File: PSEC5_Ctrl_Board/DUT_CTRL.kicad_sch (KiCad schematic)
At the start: 2 parts, among them J2 QSH-040-01-X-D-DP-A, J4 QSH-040-01-X-D-DP-A

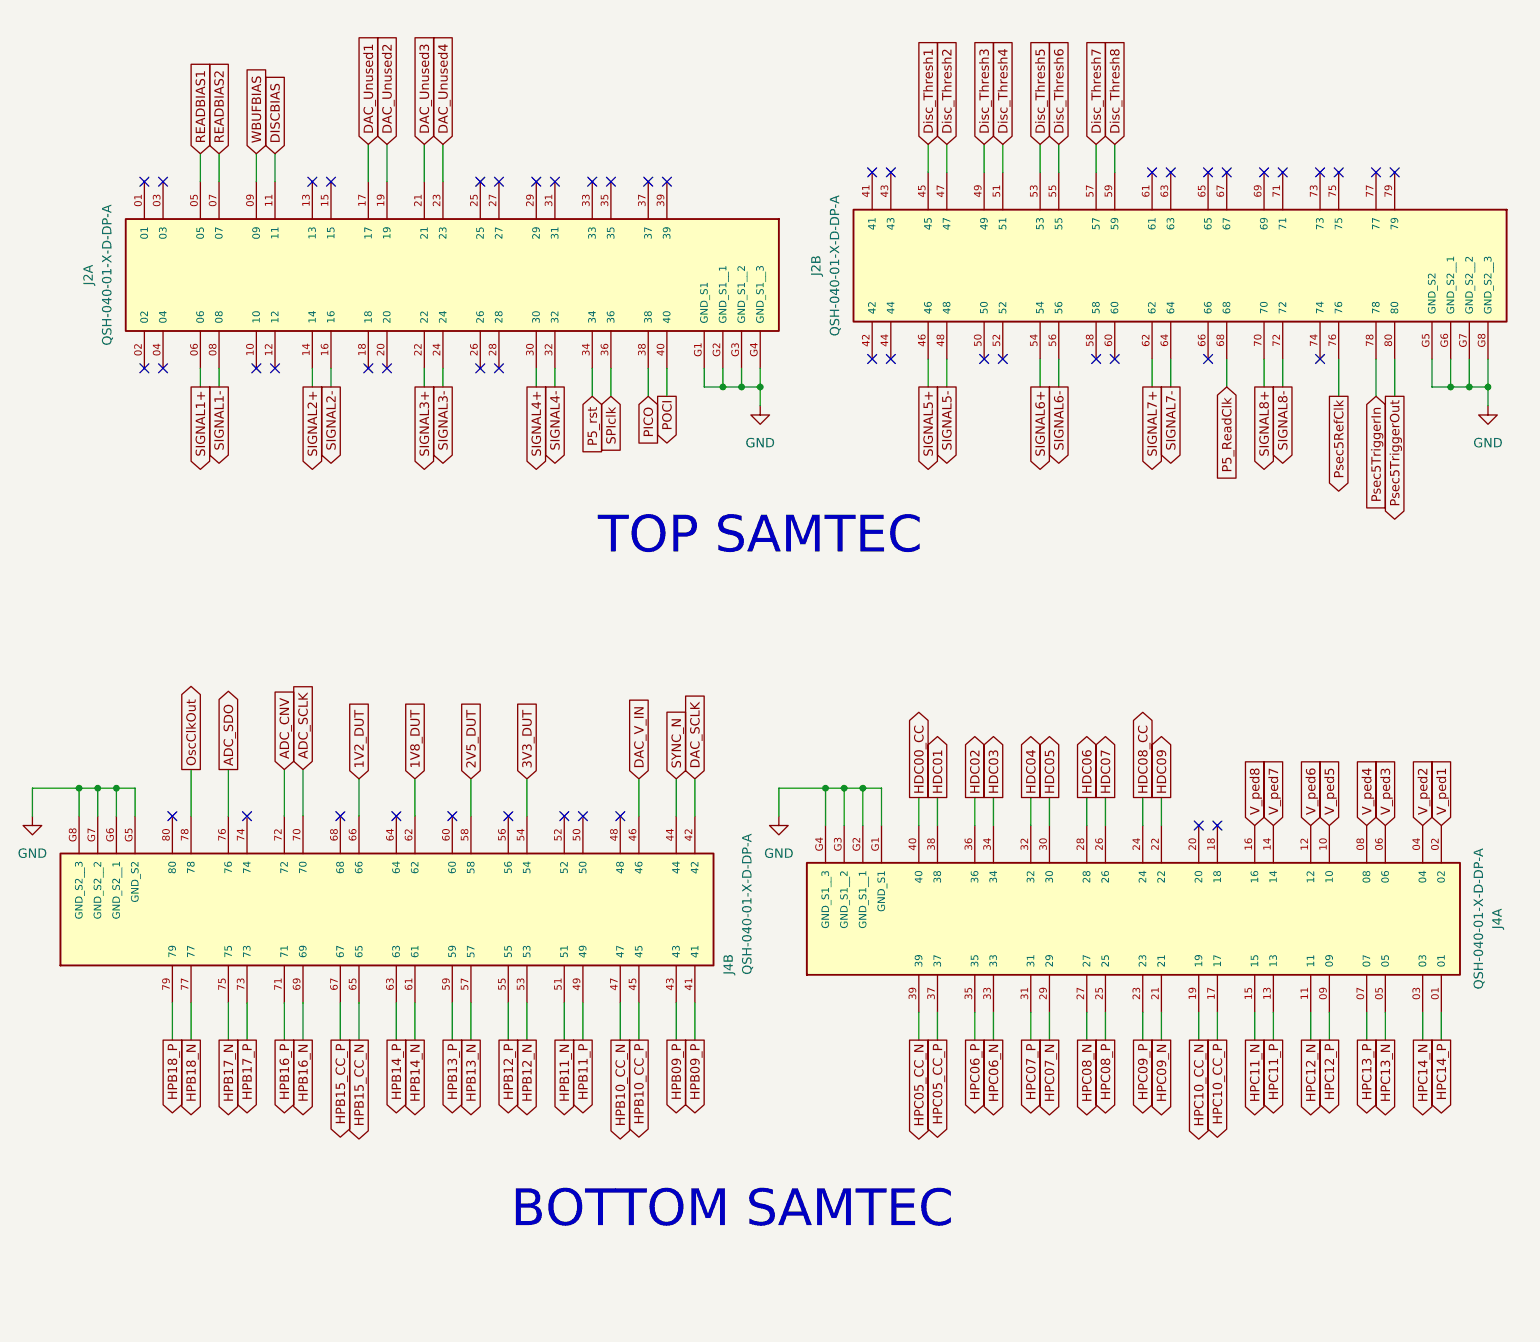
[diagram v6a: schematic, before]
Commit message: Changed Buck Regulators to external
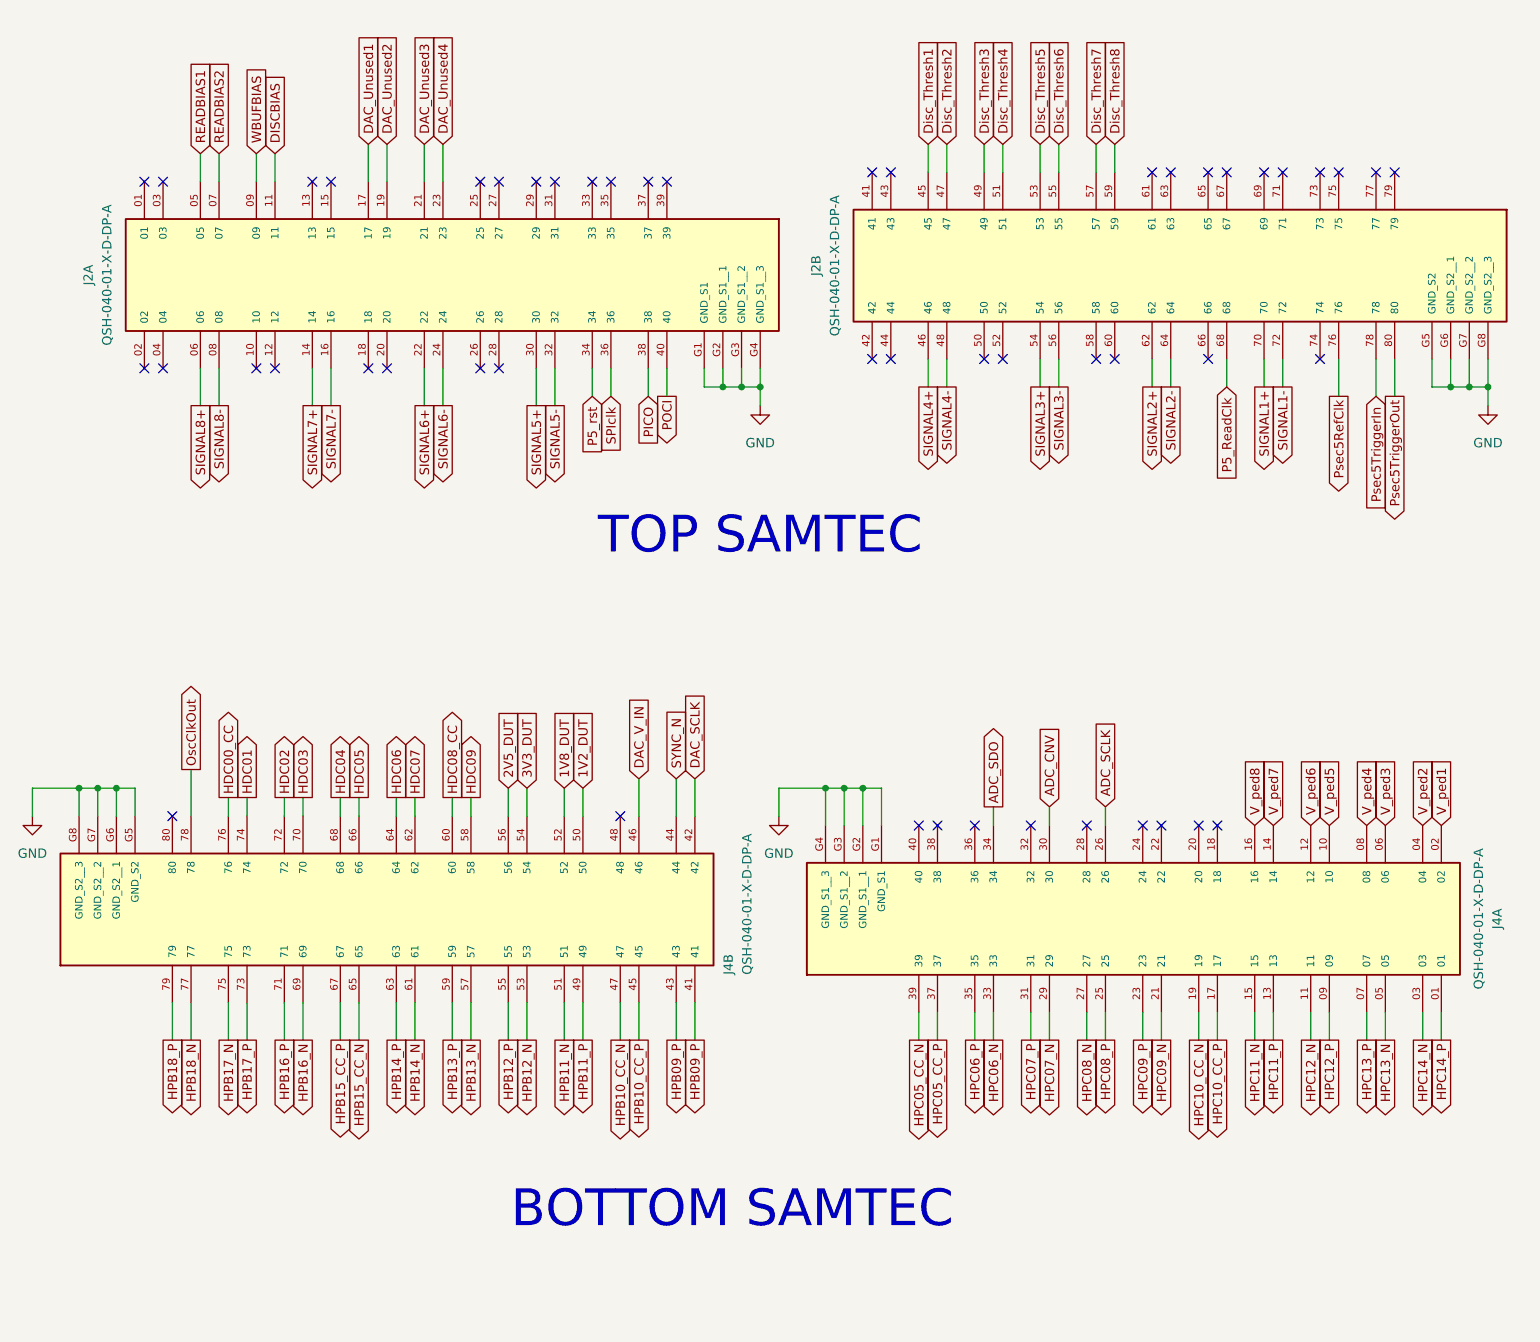
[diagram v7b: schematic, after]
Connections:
- net 1V2_DUT: now also J4.50; no longer J4.66
- net 1V8_DUT: now also J4.52; no longer J4.62
- net 2V5_DUT: now also J4.56; no longer J4.58
- net ADC_CNV: now also J4.30; no longer J4.72
- net ADC_SCLK: now also J4.26; no longer J4.70
- net ADC_SDO: now also J4.34; no longer J4.76
- net HDC00_CC: now also J4.76; no longer J4.40
- net HDC01: now also J4.74; no longer J4.38
- net HDC02: now also J4.72; no longer J4.36
- net HDC03: now also J4.70; no longer J4.34
- net HDC04: now also J4.68; no longer J4.32
- net HDC05: now also J4.66; no longer J4.30
- net HDC06: now also J4.64; no longer J4.28
- net HDC07: now also J4.62; no longer J4.26
- net HDC08_CC: now also J4.60; no longer J4.24
- net HDC09: now also J4.58; no longer J4.22
- net SIGNAL1+: now also J2.70; no longer J2.06
- net SIGNAL1-: now also J2.72; no longer J2.08
- net SIGNAL2+: now also J2.62; no longer J2.14
- net SIGNAL2-: now also J2.64; no longer J2.16
- net SIGNAL3+: now also J2.54; no longer J2.22
- net SIGNAL3-: now also J2.56; no longer J2.24
- net SIGNAL4+: now also J2.46; no longer J2.30
- net SIGNAL4-: now also J2.48; no longer J2.32
- net SIGNAL5+: now also J2.30; no longer J2.46
- net SIGNAL5-: now also J2.32; no longer J2.48
- net SIGNAL6+: now also J2.22; no longer J2.54
- net SIGNAL6-: now also J2.24; no longer J2.56
- net SIGNAL7+: now also J2.14; no longer J2.62
- net SIGNAL7-: now also J2.16; no longer J2.64
- net SIGNAL8+: now also J2.06; no longer J2.70
- net SIGNAL8-: now also J2.08; no longer J2.72

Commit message: rearranged samtec
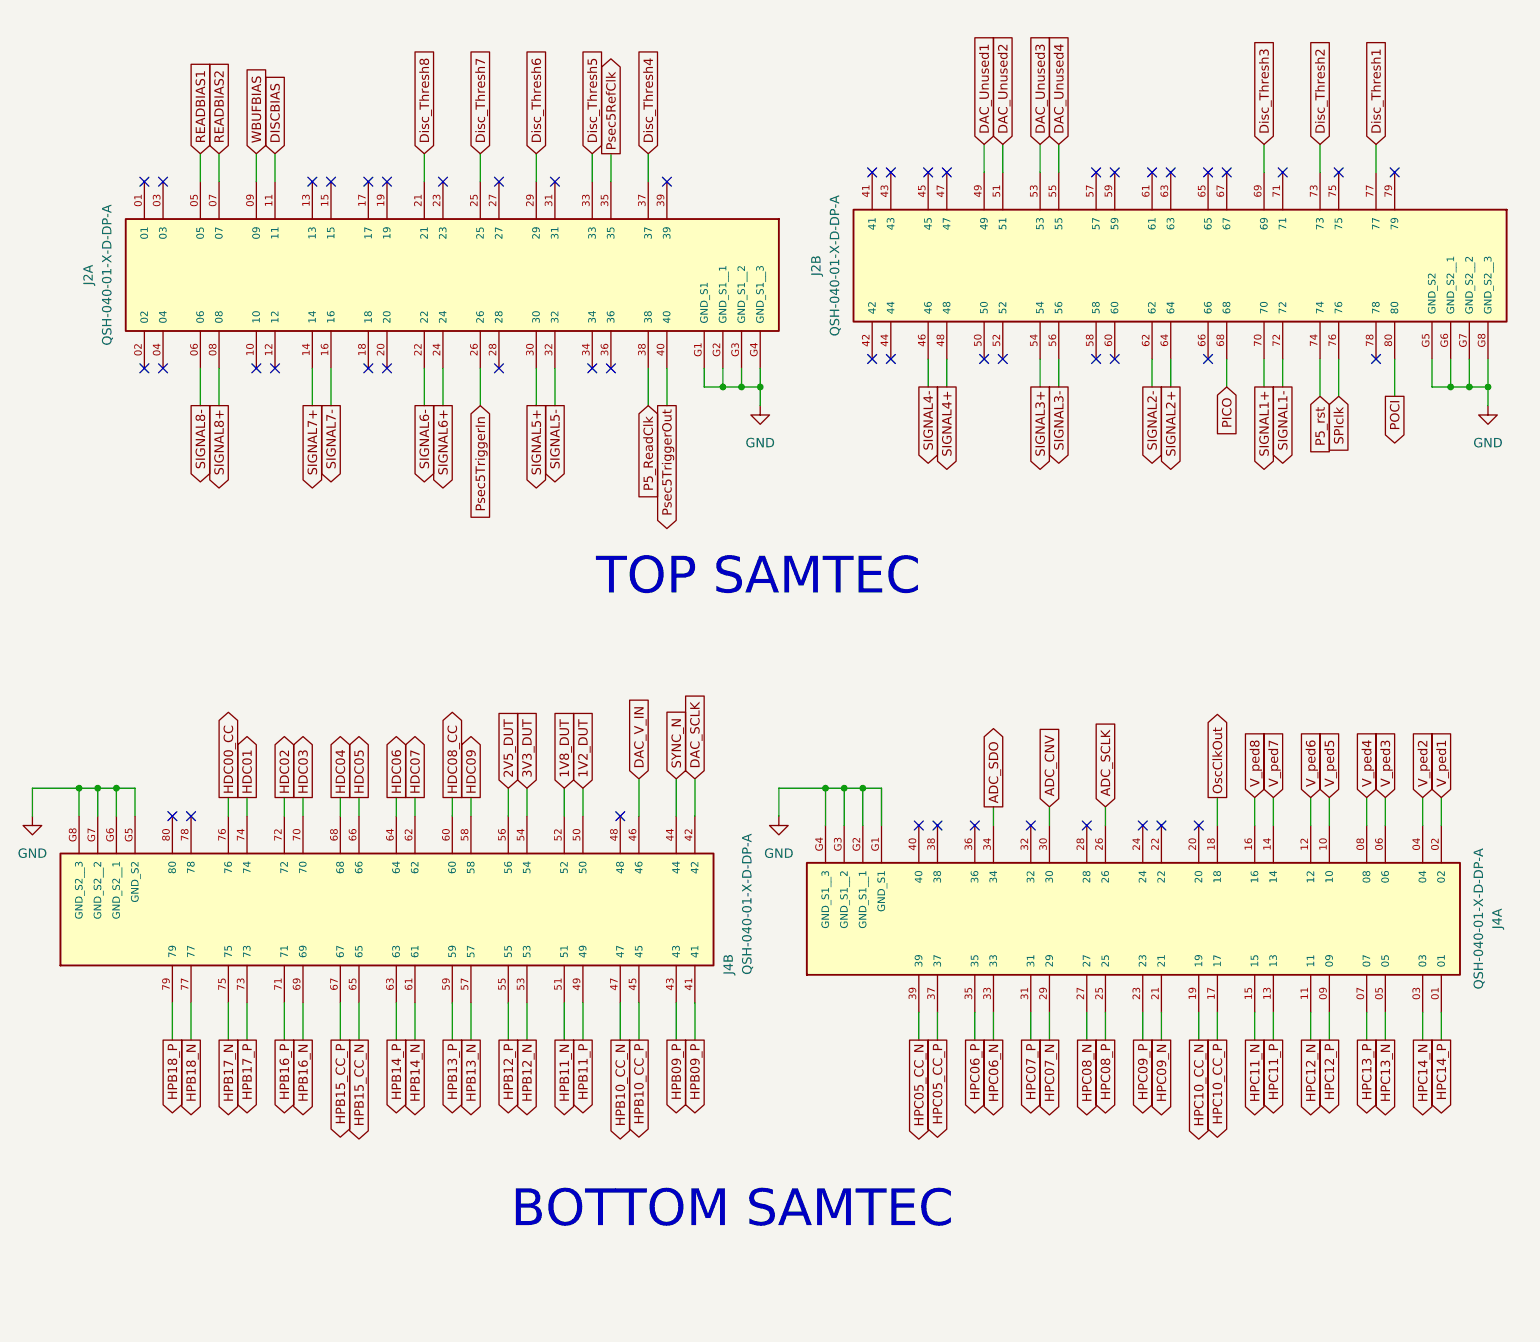
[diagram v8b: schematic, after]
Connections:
- net DAC_Unused1: now also J2.49; no longer J2.17
- net DAC_Unused2: now also J2.51; no longer J2.19
- net DAC_Unused3: now also J2.53; no longer J2.21
- net DAC_Unused4: now also J2.55; no longer J2.23
- net Disc_Thresh1: now also J2.77; no longer J2.45
- net Disc_Thresh2: now also J2.73; no longer J2.47
- net Disc_Thresh3: now also J2.69; no longer J2.49
- net Disc_Thresh4: now also J2.37; no longer J2.51
- net Disc_Thresh5: now also J2.33; no longer J2.53
- net Disc_Thresh6: now also J2.29; no longer J2.55
- net Disc_Thresh7: now also J2.25; no longer J2.57
- net Disc_Thresh8: now also J2.21; no longer J2.59
- net OscClkOut: now also J4.18; no longer J4.78
- net P5_ReadClk: now also J2.38; no longer J2.68
- net P5_rst: now also J2.74; no longer J2.34
- net PICO: now also J2.68; no longer J2.38
- net POCI: now also J2.80; no longer J2.40
- net Psec5RefClk: now also J2.35; no longer J2.76
- net Psec5TriggerIn: now also J2.26; no longer J2.78
- net Psec5TriggerOut: now also J2.40; no longer J2.80
- net SIGNAL2+: now also J2.64; no longer J2.62
- net SIGNAL2-: now also J2.62; no longer J2.64
- net SIGNAL4+: now also J2.48; no longer J2.46
- net SIGNAL4-: now also J2.46; no longer J2.48
- net SIGNAL6+: now also J2.24; no longer J2.22
- net SIGNAL6-: now also J2.22; no longer J2.24
- net SIGNAL8+: now also J2.08; no longer J2.06
- net SIGNAL8-: now also J2.06; no longer J2.08
- net SPIclk: now also J2.76; no longer J2.36
